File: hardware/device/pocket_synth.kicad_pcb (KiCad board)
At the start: 4 copper layers, 74 x 138 mm, 105 parts, among them IC1 IS42S16160J-7TLI, J1 POT_CONN, J10 MIDI_OUT, J2 USB, J3 Micro_SD_Card_Det_Hirose_DM3AT, J4 FX6-20P-0.8SV1(71), J6 LINE_IN, J8 LINE_OUT, J9 MIDI_IN, SW1 TRIG1, SW10 TRIG10, SW11 TRIG11, SW12 TRIG12, SW13 TRIG13, SW14 TRIG14, SW15 TRIG15, SW16 TRIG16, SW17 KMR221NGLFS, SW18 HELP, SW2 TRIG2, SW3 TRIG3, SW4 TRIG4, SW5 TRIG5, SW6 TRIG6, SW7 TRIG7, SW8 TRIG8, SW9 TRIG9, U1 VOL_PWR_POT, U10 TRIG9, U11 TRIG13, U12 TRIG10, U13 TRIG14, U14 TRIG11, U15 TRIG15, U16 TRIG12, U17 TRIG16, U18 STM32H743ZIT6, U19 ER-TFT024IPS-3, U2 TRIG1, U20 TPS62A02DRL, U21 TPS560200, U22 MAX17261xxTD, U23 BQ21040DBV, U25 TCA8418RTWR, U26 FUSB303BTMX, U27 FUSB302B01MPX, U3 TRIG2, U4 TRIG3, U5 TRIG4, U6 TRIG8, U7 TRIG7, U8 TRIG6, U9 TRIG5

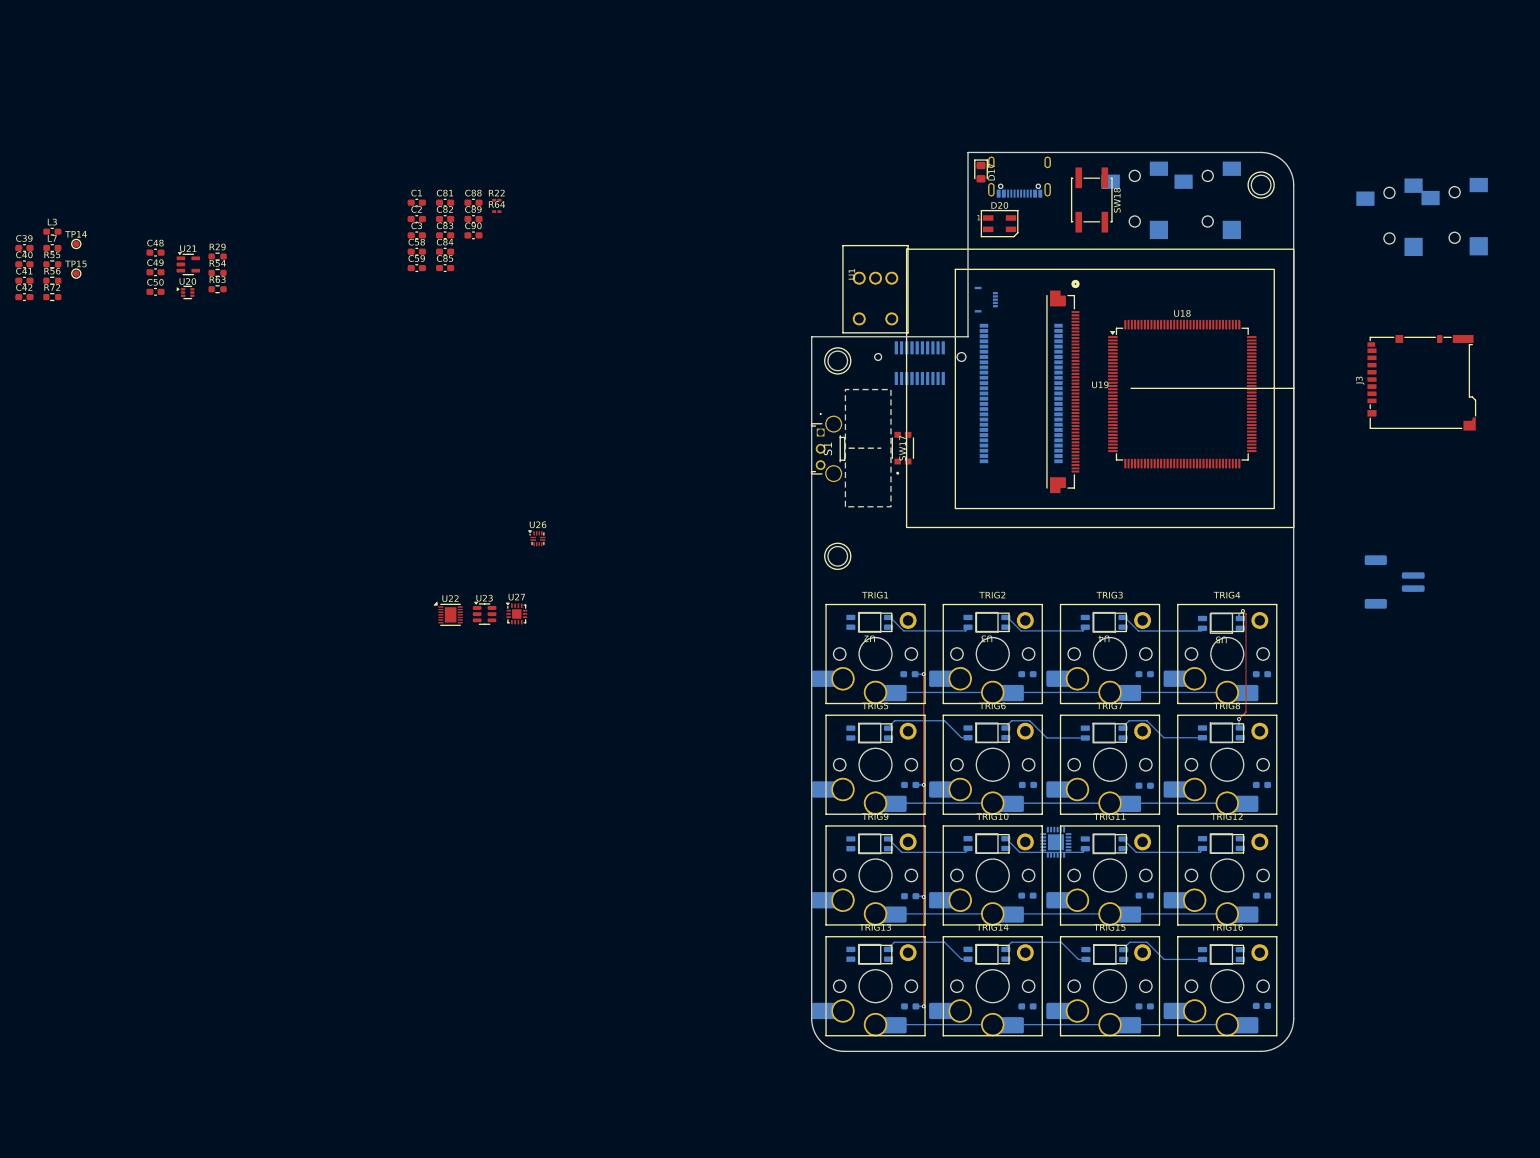
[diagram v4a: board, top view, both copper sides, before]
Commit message: feat: audio schematic, FMC bus, SDRAM connections
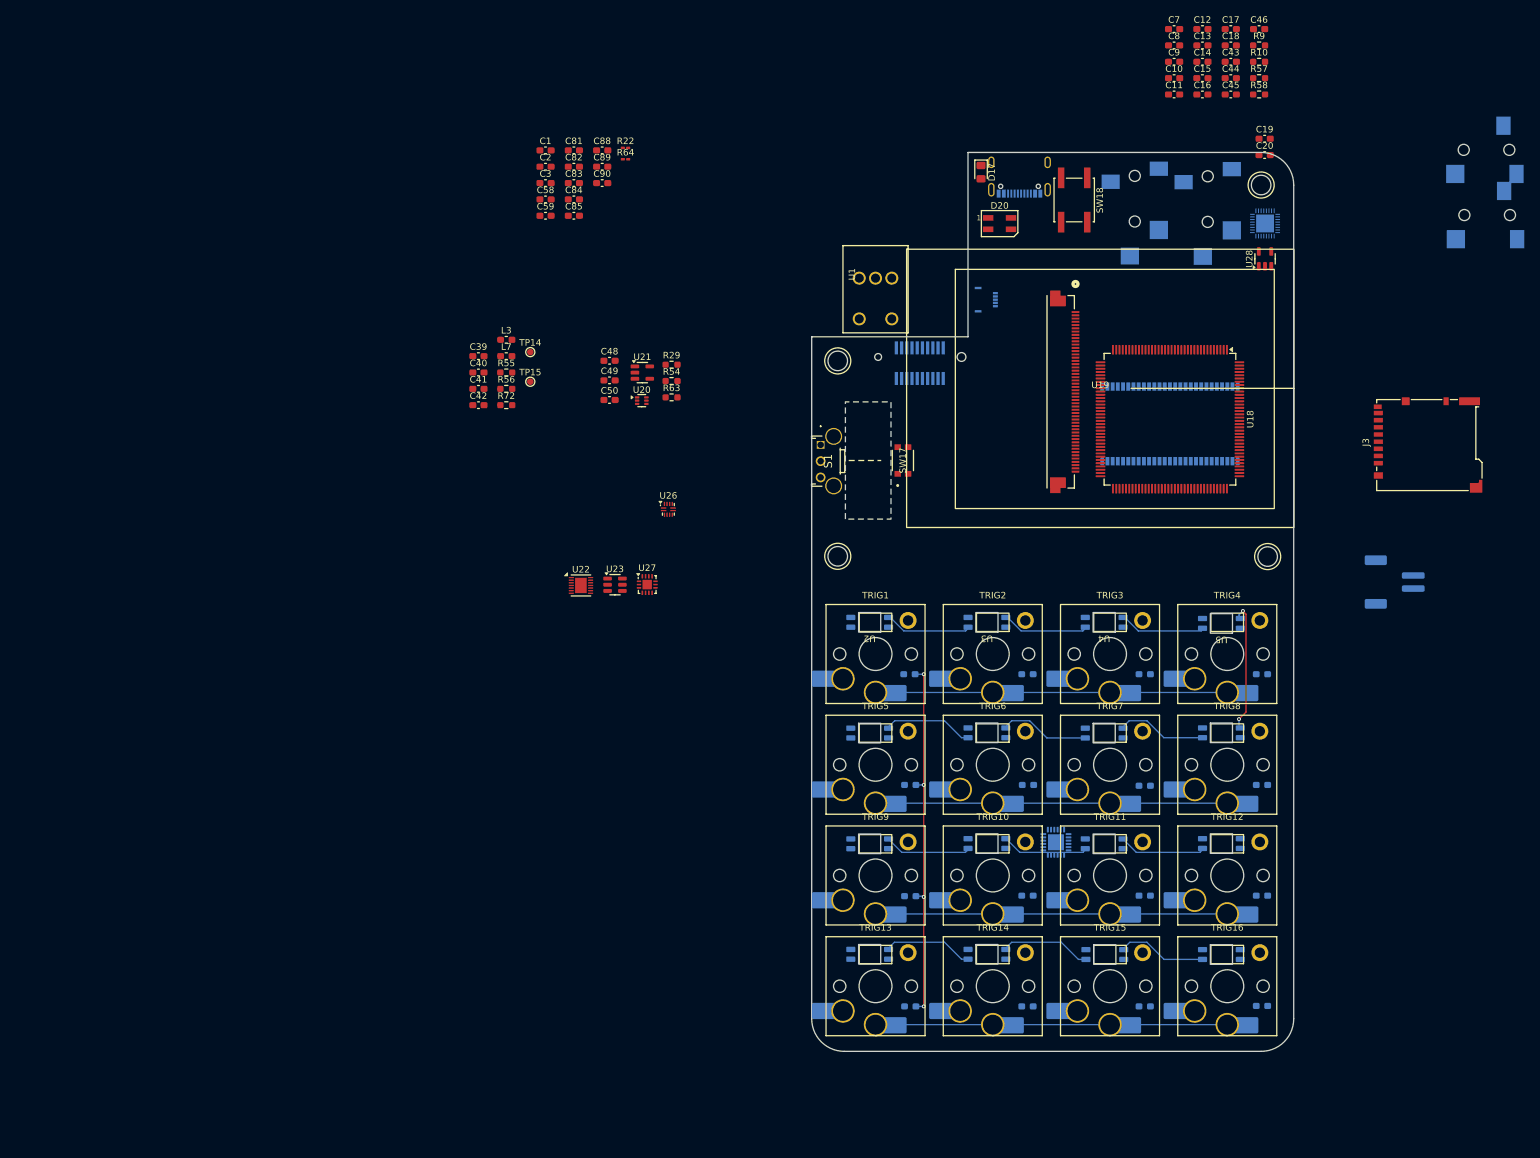
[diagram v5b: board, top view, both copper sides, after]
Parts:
- removed J8: LINE_OUT, Connector_Audio:Jack_3.5mm_CUI_SJ-3523-SMT_Horizontal
- added C10: 2.2uF, Capacitor_SMD:C_0603_1608Metric_Pad1.08x0.95mm_HandSolder, F.Cu at (85.6, 18.6)
- added C11: 2.2uF, Capacitor_SMD:C_0603_1608Metric_Pad1.08x0.95mm_HandSolder, F.Cu at (85.6, 21.1)
- added C12: 4.7uF, Capacitor_SMD:C_0603_1608Metric_Pad1.08x0.95mm_HandSolder, F.Cu at (90.0, 11.1)
- added C13: 4.7uF, Capacitor_SMD:C_0603_1608Metric_Pad1.08x0.95mm_HandSolder, F.Cu at (90.0, 13.6)
- added C14: 0.1uF, Capacitor_SMD:C_0603_1608Metric_Pad1.08x0.95mm_HandSolder, F.Cu at (90.0, 16.1)
- added C15: 4.7uF, Capacitor_SMD:C_0603_1608Metric_Pad1.08x0.95mm_HandSolder, F.Cu at (90.0, 18.6)
- added C16: 4.7uF, Capacitor_SMD:C_0603_1608Metric_Pad1.08x0.95mm_HandSolder, F.Cu at (90.0, 21.1)
- added C17: 0.1uF, Capacitor_SMD:C_0603_1608Metric_Pad1.08x0.95mm_HandSolder, F.Cu at (94.3, 11.1)
- added C18: 0.1uF, Capacitor_SMD:C_0603_1608Metric_Pad1.08x0.95mm_HandSolder, F.Cu at (94.3, 13.6)
- added C19: 1uF, Capacitor_SMD:C_0603_1608Metric_Pad1.08x0.95mm_HandSolder, F.Cu at (99.5, 27.9)
- added C20: 1uF, Capacitor_SMD:C_0603_1608Metric_Pad1.08x0.95mm_HandSolder, F.Cu at (99.5, 30.4)
- added C43: 10uf, Capacitor_SMD:C_0603_1608Metric_Pad1.08x0.95mm_HandSolder, F.Cu at (94.3, 16.1)
- added C44: 0.1uf, Capacitor_SMD:C_0603_1608Metric_Pad1.08x0.95mm_HandSolder, F.Cu at (94.3, 18.6)
- added C45: 10uf, Capacitor_SMD:C_0603_1608Metric_Pad1.08x0.95mm_HandSolder, F.Cu at (94.3, 21.1)
- added C46: 10uf, Capacitor_SMD:C_0603_1608Metric_Pad1.08x0.95mm_HandSolder, F.Cu at (98.7, 11.1)
- added C7: 0.1uF, Capacitor_SMD:C_0603_1608Metric_Pad1.08x0.95mm_HandSolder, F.Cu at (85.6, 11.1)
- added C8: 0.1uF, Capacitor_SMD:C_0603_1608Metric_Pad1.08x0.95mm_HandSolder, F.Cu at (85.6, 13.6)
- added C9: 2.2uF, Capacitor_SMD:C_0603_1608Metric_Pad1.08x0.95mm_HandSolder, F.Cu at (85.6, 16.1)
- added J7: LINE_OUT, Connector_Audio:Jack_3.5mm_CUI_SJ-3524-SMT_Horizontal, B.Cu at (79.6, 36.1)
- added R10: 20R, Resistor_SMD:R_0603_1608Metric_Pad0.98x0.95mm_HandSolder, F.Cu at (98.7, 16.1)
- added R57: 24.9k, Resistor_SMD:R_0603_1608Metric_Pad0.98x0.95mm_HandSolder, F.Cu at (98.7, 18.6)
- added R58: 20.0k, Resistor_SMD:R_0603_1608Metric_Pad0.98x0.95mm_HandSolder, F.Cu at (98.7, 21.1)
- added R9: 20R, Resistor_SMD:R_0603_1608Metric_Pad0.98x0.95mm_HandSolder, F.Cu at (98.7, 13.6)
- added U24: WM8904CGEFL/RV, pocket_synth:WM8904CGEFL_RV, B.Cu at (99.6, 40.9)
- added U28: TPS560200, Package_TO_SOT_SMD:SOT-23-5, F.Cu at (99.6, 46.3)
- J4: value FX6-20P-0.8SV1(71) -> EXPANSION
- J6: footprint Connector_Audio:Jack_3.5mm_CUI_SJ-3523-SMT_Horizontal -> Connector_Audio:Jack_3.5mm_CUI_SJ-3524-SMT_Horizontal
- moved C41 71.6 mm to (-21.2, 66.3)
- moved C48 71.6 mm to (-1.04, 62.0)
- moved C49 71.6 mm to (-1.04, 65.0)
- moved C50 71.6 mm to (-1.04, 68.0)
- moved L3 71.6 mm to (-16.9, 58.8)
- moved L7 71.6 mm to (-16.9, 61.3)
- moved R29 71.6 mm to (8.49, 62.6)
- moved R54 71.6 mm to (8.49, 65.1)
- moved R55 71.6 mm to (-16.9, 63.8)
- moved R56 71.6 mm to (-16.9, 66.3)
- moved R63 71.6 mm to (8.49, 67.6)
- moved R72 71.6 mm to (-16.9, 68.8)
- moved TP14 71.6 mm to (-13.2, 60.6)
- moved TP15 71.6 mm to (-13.2, 65.2)
- moved U21 71.6 mm to (4.00, 63.8)
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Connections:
- net /BOOT0 renamed /MCU/BOOT0
- net /SWD_RESET renamed /MCU/SWD_RESET
- IC1 pad 10: unconnected-(IC1-DQ5-Pad10) -> /Display/FMC.D5
- IC1 pad 11: unconnected-(IC1-DQ6-Pad11) -> /Display/FMC.D6
- IC1 pad 13: unconnected-(IC1-DQ7-Pad13) -> /Display/FMC.D7
- IC1 pad 15: unconnected-(IC1-DQML-Pad15) -> /Display/FMC.DQML
- IC1 pad 16: unconnected-(IC1-~{WE}-Pad16) -> /Display/FMC.NWE
- IC1 pad 17: unconnected-(IC1-~{CAS}-Pad17) -> /Display/FMC.CAS
- IC1 pad 18: unconnected-(IC1-~{RAS}-Pad18) -> /Display/FMC.RAS
- IC1 pad 19: unconnected-(IC1-~{CS}-Pad19) -> /Display/FMC.NE0
- IC1 pad 2: unconnected-(IC1-DQ0-Pad2) -> /Display/FMC.D0
- IC1 pad 20: unconnected-(IC1-BA0-Pad20) -> /Display/FMC.BA0
- IC1 pad 21: unconnected-(IC1-BA1-Pad21) -> /Display/FMC.BA1
- IC1 pad 22: unconnected-(IC1-A10-Pad22) -> /Display/FMC.A10
- IC1 pad 23: unconnected-(IC1-A0-Pad23) -> /Display/FMC.A0
- IC1 pad 24: unconnected-(IC1-A1-Pad24) -> /Display/FMC.A1
- IC1 pad 25: unconnected-(IC1-A2-Pad25) -> /Display/FMC.A2
- IC1 pad 26: unconnected-(IC1-A3-Pad26) -> /Display/FMC.A3
- IC1 pad 29: unconnected-(IC1-A4-Pad29) -> /Display/FMC.A4
- IC1 pad 30: unconnected-(IC1-A5-Pad30) -> /Display/FMC.A5
- IC1 pad 31: unconnected-(IC1-A6-Pad31) -> /Display/FMC.A6
- IC1 pad 32: unconnected-(IC1-A7-Pad32) -> /Display/FMC.A7
- IC1 pad 33: unconnected-(IC1-A8-Pad33) -> /Display/FMC.A8
- IC1 pad 34: unconnected-(IC1-A9-Pad34) -> /Display/FMC.A9
- IC1 pad 35: unconnected-(IC1-A11-Pad35) -> /Display/FMC.A11
- IC1 pad 36: unconnected-(IC1-A12-Pad36) -> /Display/FMC.A12
- IC1 pad 37: unconnected-(IC1-CKE-Pad37) -> /Display/FMC.CKE
- IC1 pad 38: unconnected-(IC1-CLK-Pad38) -> /Display/FMC.CLK
- IC1 pad 39: unconnected-(IC1-DQMH-Pad39) -> /Display/FMC.DQMH
- IC1 pad 4: unconnected-(IC1-DQ1-Pad4) -> /Display/FMC.D1
- IC1 pad 42: unconnected-(IC1-DQ8-Pad42) -> /Display/FMC.D8
- IC1 pad 44: unconnected-(IC1-DQ9-Pad44) -> /Display/FMC.D9
- IC1 pad 45: unconnected-(IC1-DQ10-Pad45) -> /Display/FMC.D10
- IC1 pad 47: unconnected-(IC1-DQ11-Pad47) -> /Display/FMC.D11
- IC1 pad 48: unconnected-(IC1-DQ12-Pad48) -> /Display/FMC.D12
- IC1 pad 5: unconnected-(IC1-DQ2-Pad5) -> /Display/FMC.D2
- IC1 pad 50: unconnected-(IC1-DQ13-Pad50) -> /Display/FMC.D13
- IC1 pad 51: unconnected-(IC1-DQ14-Pad51) -> /Display/FMC.D14
- IC1 pad 53: unconnected-(IC1-DQ15-Pad53) -> /Display/FMC.D15
- IC1 pad 7: unconnected-(IC1-DQ3-Pad7) -> /Display/FMC.D3
- IC1 pad 8: unconnected-(IC1-DQ4-Pad8) -> /Display/FMC.D4
- J4 pad 1: unconnected-(J4-Pad1) -> +3.3V
- J4 pad 11: unconnected-(J4-Pad11) -> /MCU/EXP_I2S_DIN
- J4 pad 13: unconnected-(J4-Pad13) -> /MCU/EXP_I2S_DOUT
- J4 pad 15: unconnected-(J4-Pad15) -> /MCU/EXP_I2S_CLK
- J4 pad 17: unconnected-(J4-Pad17) -> /MCU/EXP_INT1
- J4 pad 19: unconnected-(J4-Pad19) -> GND
- J4 pad 2: unconnected-(J4-Pad2) -> /MCU/EXP_DETECT
- J4 pad 3: unconnected-(J4-Pad3) -> VDD
- J4 pad 5: unconnected-(J4-Pad5) -> /MCU/EXP_UART_RX
- J4 pad 7: unconnected-(J4-Pad7) -> /MCU/EXP_UART_TX
- J4 pad 9: unconnected-(J4-Pad9) -> /MCU/EXP_I2S_WCLK
- J6 pad R: unconnected-(J6-PadR) -> Net-(C19-Pad1)
- J6 pad S: unconnected-(J6-PadS) -> GND
- J6 pad T: unconnected-(J6-PadT) -> Net-(C20-Pad1)
- U18 pad 10: unconnected-(U18F-PF0-Pad10) -> /Display/FMC.A0
- U18 pad 11: unconnected-(U18F-PF1-Pad11) -> /Display/FMC.A1
- U18 pad 114: unconnected-(U18D-PD0-Pad114) -> /Display/FMC.D2
- U18 pad 115: unconnected-(U18D-PD1-Pad115) -> /Display/FMC.D3
- U18 pad 118: unconnected-(U18D-PD4-Pad118) -> /Display/FMC.NOE
- U18 pad 119: unconnected-(U18D-PD5-Pad119) -> /Display/FMC.NWE
- U18 pad 12: unconnected-(U18F-PF2-Pad12) -> /Display/FMC.A2
- U18 pad 13: unconnected-(U18F-PF3-Pad13) -> /Display/FMC.A3
- U18 pad 132: unconnected-(U18G-PG15-Pad132) -> /Display/FMC.CAS
- U18 pad 14: unconnected-(U18F-PF4-Pad14) -> /Display/FMC.A4
- U18 pad 141: unconnected-(U18E-PE0-Pad141) -> /Display/FMC.DQML
- U18 pad 142: unconnected-(U18E-PE1-Pad142) -> /Display/FMC.DQMH
- U18 pad 15: unconnected-(U18F-PF5-Pad15) -> /Display/FMC.A5
- U18 pad 26: unconnected-(U18C-PC0-Pad26) -> /Display/FMC.NWE
- U18 pad 28: unconnected-(U18C-PC2_C-Pad28) -> /Display/FMC.NE0
- U18 pad 29: unconnected-(U18C-PC3_C-Pad29) -> /Display/FMC.CKE
- U18 pad 49: unconnected-(U18F-PF11-Pad49) -> /Display/FMC.RAS
- U18 pad 50: unconnected-(U18F-PF12-Pad50) -> /Display/FMC.A6
- U18 pad 53: unconnected-(U18F-PF13-Pad53) -> /Display/FMC.A7
- U18 pad 54: unconnected-(U18F-PF14-Pad54) -> /Display/FMC.A8
- U18 pad 55: unconnected-(U18F-PF15-Pad55) -> /Display/FMC.A9
- U18 pad 56: unconnected-(U18G-PG0-Pad56) -> /Display/FMC.A10
- U18 pad 57: unconnected-(U18G-PG1-Pad57) -> /Display/FMC.A11
- U18 pad 58: unconnected-(U18E-PE7-Pad58) -> /Display/FMC.D4
- U18 pad 59: unconnected-(U18E-PE8-Pad59) -> /Display/FMC.D5
- U18 pad 60: unconnected-(U18E-PE9-Pad60) -> /Display/FMC.D6
- U18 pad 63: unconnected-(U18E-PE10-Pad63) -> /Display/FMC.D7
- U18 pad 64: unconnected-(U18E-PE11-Pad64) -> /Display/FMC.D8
- U18 pad 65: unconnected-(U18E-PE12-Pad65) -> /Display/FMC.D9
- U18 pad 66: unconnected-(U18E-PE13-Pad66) -> /Display/FMC.D10
- U18 pad 67: unconnected-(U18E-PE14-Pad67) -> /Display/FMC.D11
- U18 pad 68: unconnected-(U18E-PE15-Pad68) -> /Display/FMC.D12
- U18 pad 77: unconnected-(U18D-PD8-Pad77) -> /Display/FMC.D13
- U18 pad 78: unconnected-(U18D-PD9-Pad78) -> /Display/FMC.D14
- U18 pad 79: unconnected-(U18D-PD10-Pad79) -> /Display/FMC.D15
- U18 pad 85: unconnected-(U18D-PD14-Pad85) -> /Display/FMC.D0
- U18 pad 86: unconnected-(U18D-PD15-Pad86) -> /Display/FMC.D1
- U18 pad 87: unconnected-(U18G-PG2-Pad87) -> /Display/FMC.A12
- U18 pad 89: unconnected-(U18G-PG4-Pad89) -> /Display/FMC.BA0
- U18 pad 90: unconnected-(U18G-PG5-Pad90) -> /Display/FMC.BA1
- U18 pad 93: unconnected-(U18G-PG8-Pad93) -> /Display/FMC.CLK
- U18 pad 97: unconnected-(U18C-PC7-Pad97) -> /Display/FMC.NE1
- U19 pad 1: unconnected-(U19A-A-Pad1) -> +3.3V
- U19 pad 11: unconnected-(U19B-VSYNC-Pad11) -> GND
- U19 pad 12: unconnected-(U19B-HSYNC-Pad12) -> GND
- U19 pad 13: unconnected-(U19B-DOTCLK-Pad13) -> GND
- U19 pad 14: unconnected-(U19B-DE-Pad14) -> GND
- U19 pad 15: unconnected-(U19B-D17-Pad15) -> GND
- U19 pad 16: unconnected-(U19B-D16-Pad16) -> GND
- U19 pad 17: unconnected-(U19B-D15-Pad17) -> /Display/FMC.D15
- U19 pad 18: unconnected-(U19B-D14-Pad18) -> /Display/FMC.D14
- U19 pad 19: unconnected-(U19B-D13-Pad19) -> /Display/FMC.D13
- U19 pad 2: unconnected-(U19A-K1-Pad2) -> Net-(U19A-K1)
- U19 pad 20: unconnected-(U19B-D12-Pad20) -> /Display/FMC.D12
- U19 pad 21: unconnected-(U19B-D11-Pad21) -> /Display/FMC.D11
- U19 pad 22: unconnected-(U19B-D10-Pad22) -> /Display/FMC.D10
- U19 pad 23: unconnected-(U19B-D9-Pad23) -> /Display/FMC.D9
- U19 pad 24: unconnected-(U19B-D8-Pad24) -> /Display/FMC.D8
- U19 pad 25: unconnected-(U19B-D7-Pad25) -> /Display/FMC.D7
- U19 pad 26: unconnected-(U19B-D6-Pad26) -> /Display/FMC.D6
- U19 pad 27: unconnected-(U19B-D5-Pad27) -> /Display/FMC.D5
- U19 pad 28: unconnected-(U19B-D4-Pad28) -> /Display/FMC.D4
- U19 pad 29: unconnected-(U19B-D3-Pad29) -> /Display/FMC.D3
- U19 pad 3: unconnected-(U19A-K2-Pad3) -> Net-(U19A-K2)
- U19 pad 30: unconnected-(U19B-D2-Pad30) -> /Display/FMC.D2
- U19 pad 31: unconnected-(U19B-D1-Pad31) -> /Display/FMC.D1
- U19 pad 32: unconnected-(U19B-D0-Pad32) -> /Display/FMC.D0
- U19 pad 35: unconnected-(U19B-RDx-Pad35) -> /Display/FMC.NOE
- U19 pad 36: unconnected-(U19B-WRx-Pad36) -> /Display/FMC.NWE
- U19 pad 37: unconnected-(U19B-DCx-Pad37) -> /Display/FMC.A0
- U19 pad 38: unconnected-(U19B-CSx-Pad38) -> /Display/FMC.NE1
- U19 pad 39: unconnected-(U19B-TE-Pad39) -> GND
- U19 pad 4: unconnected-(U19A-K3-Pad4) -> Net-(U19A-K3)
- U19 pad 40: unconnected-(U19B-VDDI-Pad40) -> +3.3V
- U19 pad 41: unconnected-(U19B-VDDI-Pad41) -> +3.3V
- U19 pad 42: unconnected-(U19B-VCI-Pad42) -> +3.3V
- U19 pad 43: unconnected-(U19B-GND-Pad43) -> GND
- U19 pad 48: unconnected-(U19B-GND-Pad48) -> GND
- U19 pad 49: unconnected-(U19B-GND-Pad49) -> GND
- U19 pad 5: unconnected-(U19A-K4-Pad5) -> Net-(U19A-K4)
- U19 pad 50: unconnected-(U19B-GND-Pad50) -> GND
- U19 pad 6: unconnected-(U19B-MODE0-Pad6) -> +3.3V
- U19 pad 7: unconnected-(U19B-MODE1-Pad7) -> GND
- U19 pad 8: unconnected-(U19B-MODE2-Pad8) -> GND
- U19 pad 9: unconnected-(U19B-MODE3-Pad9) -> GND
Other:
- outline, holes or cut-outs redrawn
